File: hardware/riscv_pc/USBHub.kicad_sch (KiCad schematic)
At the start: 8 parts, among them U4 SL2.1A, X1 X49SD12MSD2SC

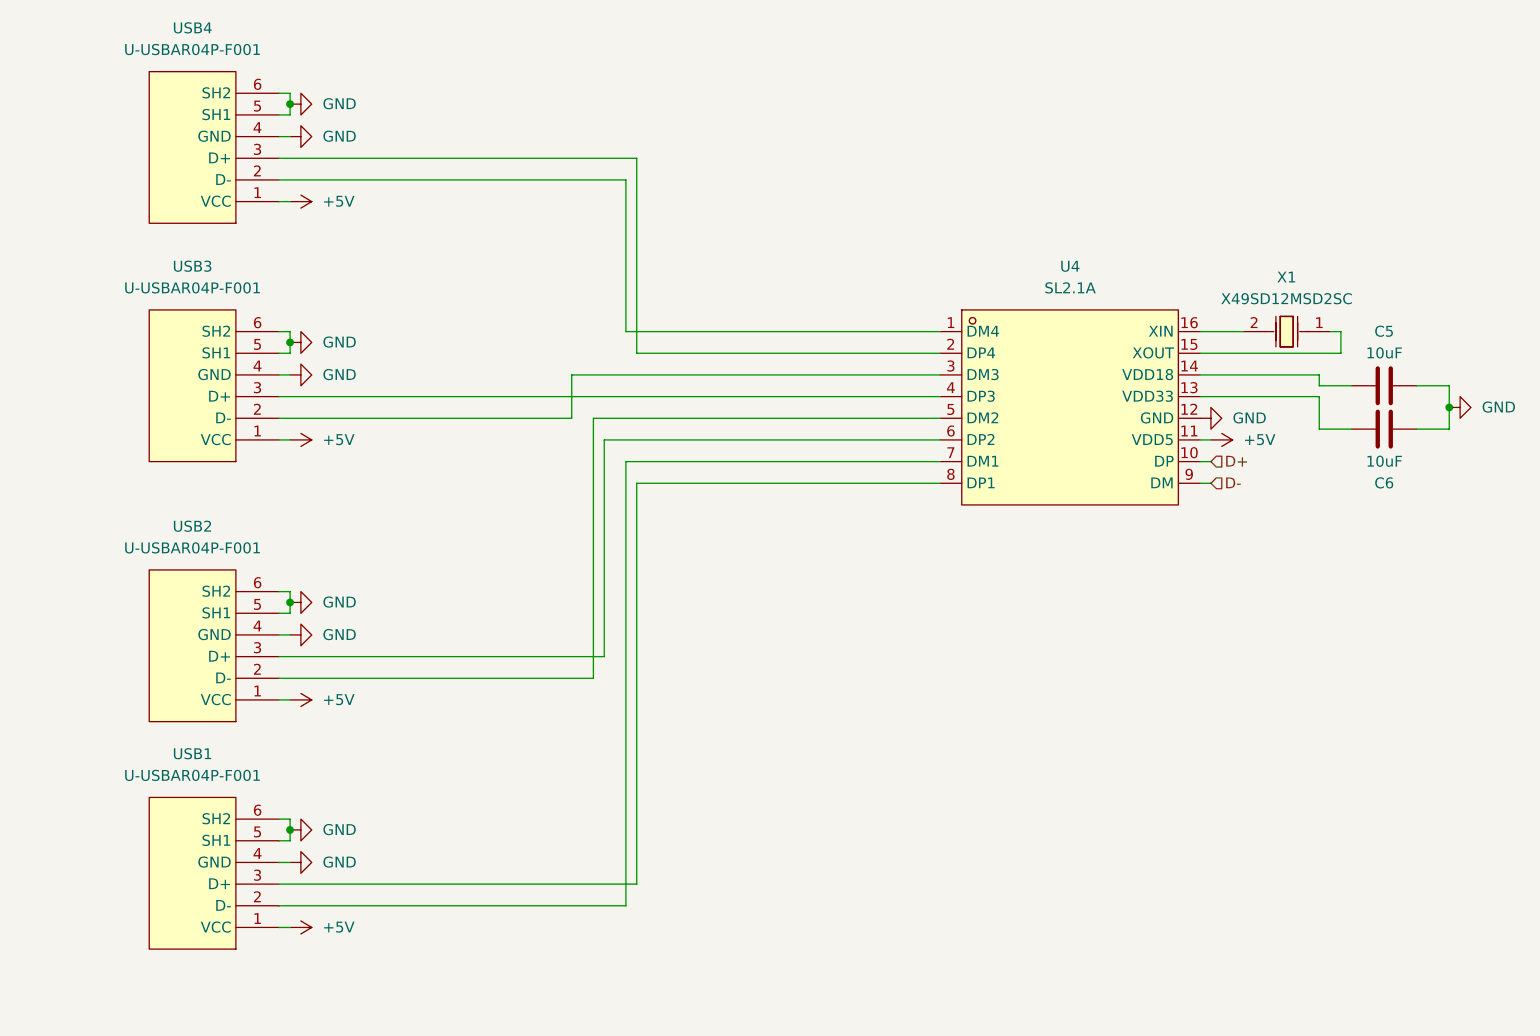
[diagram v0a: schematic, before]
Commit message: Add ESD protection to USB Lines
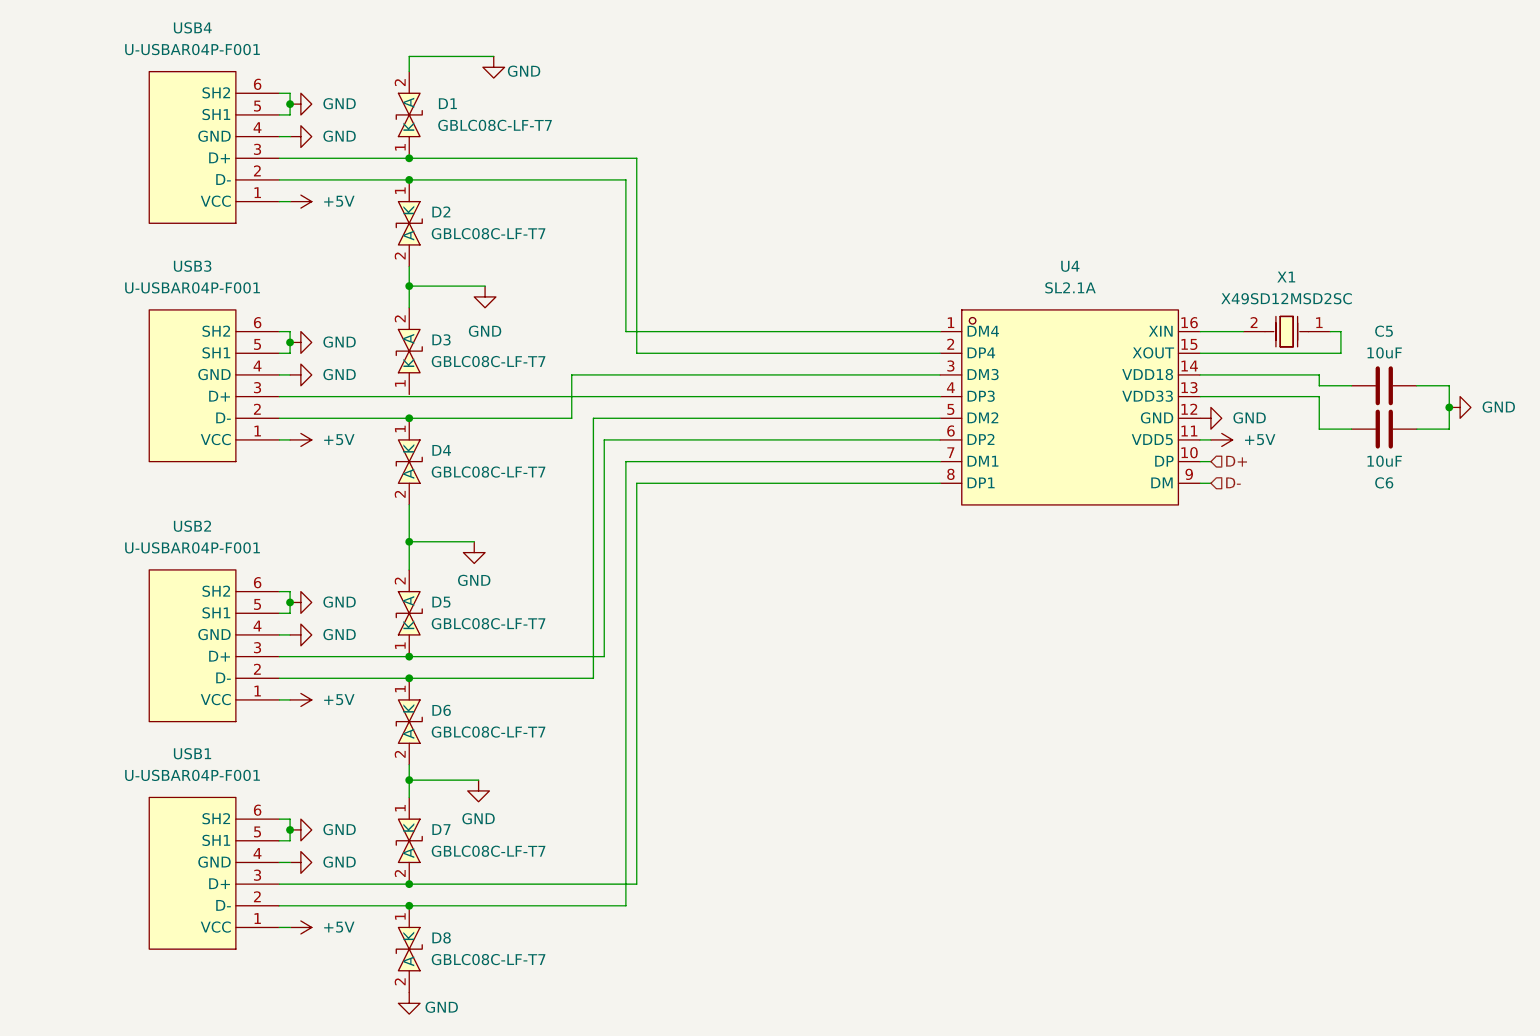
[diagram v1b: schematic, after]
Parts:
- added D1, D2, D3, D4, D5, D6, D7, D8: GBLC08C-LF-T7, easyeda2kicad:SOD-323_L1.8-W1.3-LS2.5-BI, symbol lcsc:GBLC08C-LF-T7
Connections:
- net GND: now also D1.2 (A), D2.2 (A), D3.2 (A), D4.2 (A), D5.2 (A), D6.2 (A), D7.1 (K), D8.2 (A)
- net at U4.7 (DM1), USB1.2 (D-): now also D8.1 (K)
- net at U4.8 (DP1), USB1.3 (D+): now also D7.2 (A)
- net at U4.1 (DM4), USB4.2 (D-): now also D2.1 (K)
- net at U4.2 (DP4), USB4.3 (D+): now also D1.1 (K)
- net at U4.5 (DM2), USB2.2 (D-): now also D6.1 (K)
- net at U4.6 (DP2), USB2.3 (D+): now also D5.1 (K)
- net at U4.3 (DM3), USB3.2 (D-): now also D4.1 (K)

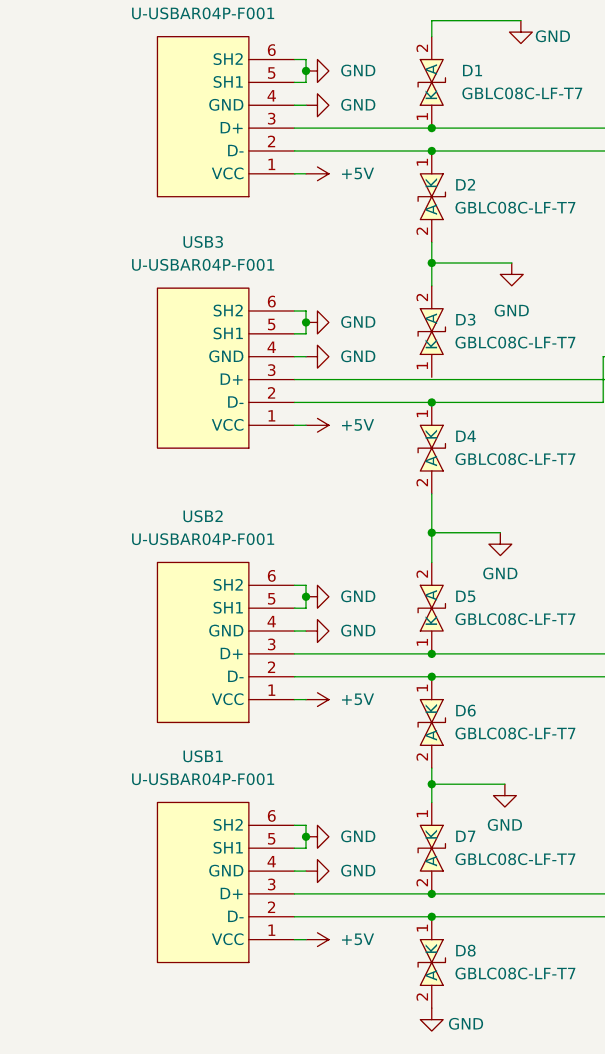
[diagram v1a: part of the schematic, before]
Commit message: Add ESD protection to AUX port
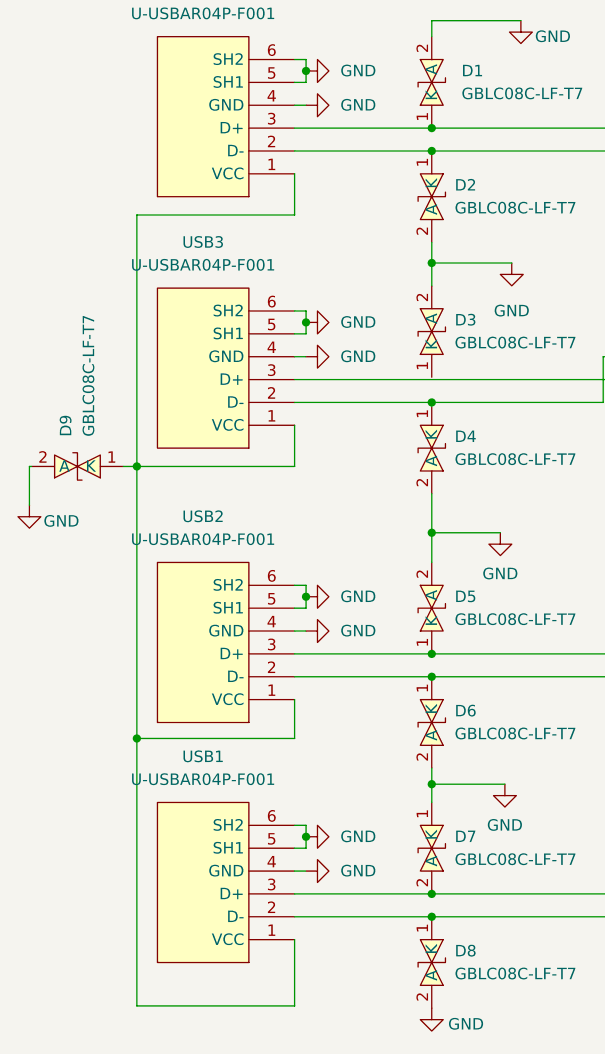
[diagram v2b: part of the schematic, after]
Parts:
- added D9: GBLC08C-LF-T7, easyeda2kicad:SOD-323_L1.8-W1.3-LS2.5-BI, symbol lcsc:GBLC08C-LF-T7
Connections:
- net +5V: no longer USB1.1 (VCC), USB2.1 (VCC), USB3.1 (VCC), USB4.1 (VCC)
- net GND: now also D9.2 (A)
- new net: D9.1 (K), USB1.1 (VCC), USB2.1 (VCC), USB3.1 (VCC), USB4.1 (VCC)
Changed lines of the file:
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@@
   (junction (at 46.99 54.61) (diameter 0) (color 0 0 0 0)
   )
+  (junction (at 28.194 100.838) (diameter 0) (color 0 0 0 0)
+  )
   (junction (at 60.96 118.11) (diameter 0) (color 0 0 0 0)
   )
@@
   (junction (at 60.96 33.02) (diameter 0) (color 0 0 0 0)
   )
+  (junction (at 28.194 70.612) (diameter 0) (color 0 0 0 0)
+  )
+  (wire (pts (xy 28.194 70.612) (xy 28.194 42.672))
+    (stroke (width 0) (type default) (color 0 0 0 0))
+  )
   (wire (pts (xy 46.99 115.57) (xy 45.72 115.57))
     (stroke (width 0) (type default) (color 0 0 0 0))
@@
     (stroke (width 0) (type default) (color 0 0 0 0))
   )
+  (wire (pts (xy 45.72 70.612) (xy 28.194 70.612))
+    (stroke (width 0) (type default) (color 0 0 0 0))
+  )
   (wire (pts (xy 87.63 71.12) (xy 87.63 118.11))
     (stroke (width 0) (type default) (color 0 0 0 0))
   )
+  (wire (pts (xy 45.72 66.04) (xy 45.72 70.612))
+    (stroke (width 0) (type default) (color 0 0 0 0))
+  )
   (wire (pts (xy 60.96 77.978) (xy 68.58 77.978))
     (stroke (width 0) (type default) (color 0 0 0 0))
@@
     (stroke (width 0) (type default) (color 0 0 0 0))
   )
+  (wire (pts (xy 45.72 42.672) (xy 45.72 38.1))
+    (stroke (width 0) (type default) (color 0 0 0 0))
+  )
   (wire (pts (xy 87.63 33.02) (xy 60.96 33.02))
     (stroke (width 0) (type default) (color 0 0 0 0))
@@
     (stroke (width 0) (type default) (color 0 0 0 0))
   )
-  (wire (pts (xy 46.99 123.19) (xy 45.72 123.19))
-    (stroke (width 0) (type default) (color 0 0 0 0))
-  )
   (wire (pts (xy 46.99 54.61) (xy 46.99 55.88))
     (stroke (width 0) (type default) (color 0 0 0 0))
   )
+  (wire (pts (xy 16.256 70.612) (xy 16.51 70.612))
+    (stroke (width 0) (type default) (color 0 0 0 0))
+  )
   (wire (pts (xy 82.55 63.5) (xy 82.55 93.98))
     (stroke (width 0) (type default) (color 0 0 0 0))
@@
     (stroke (width 0) (type default) (color 0 0 0 0))
   )
+  (wire (pts (xy 45.72 96.52) (xy 45.72 100.838))
+    (stroke (width 0) (type default) (color 0 0 0 0))
+  )
   (wire (pts (xy 167.64 58.42) (xy 167.64 59.69))
     (stroke (width 0) (type default) (color 0 0 0 0))
@@
     (stroke (width 0) (type default) (color 0 0 0 0))
   )
+  (wire (pts (xy 45.72 123.19) (xy 45.72 130.556))
+    (stroke (width 0) (type default) (color 0 0 0 0))
+  )
   (wire (pts (xy 46.99 111.76) (xy 46.99 113.03))
     (stroke (width 0) (type default) (color 0 0 0 0))
   )
-  (wire (pts (xy 46.99 38.1) (xy 45.72 38.1))
-    (stroke (width 0) (type default) (color 0 0 0 0))
-  )
   (wire (pts (xy 123.19 66.04) (xy 83.82 66.04))
     (stroke (width 0) (type default) (color 0 0 0 0))
@@
     (stroke (width 0) (type default) (color 0 0 0 0))
   )
+  (wire (pts (xy 28.194 70.612) (xy 28.194 100.838))
+    (stroke (width 0) (type default) (color 0 0 0 0))
+  )
   (wire (pts (xy 167.64 64.77) (xy 171.45 64.77))
     (stroke (width 0) (type default) (color 0 0 0 0))
@@
     (stroke (width 0) (type default) (color 0 0 0 0))
   )
+  (wire (pts (xy 16.256 74.93) (xy 16.256 70.612))
+    (stroke (width 0) (type default) (color 0 0 0 0))
+  )
   (wire (pts (xy 158.75 53.34) (xy 153.67 53.34))
     (stroke (width 0) (type default) (color 0 0 0 0))
   )
+  (wire (pts (xy 26.67 70.612) (xy 28.194 70.612))
+    (stroke (width 0) (type default) (color 0 0 0 0))
+  )
   (wire (pts (xy 123.19 68.58) (xy 86.36 68.58))
     (stroke (width 0) (type default) (color 0 0 0 0))
   )
+  (wire (pts (xy 45.72 100.838) (xy 28.194 100.838))
+    (stroke (width 0) (type default) (color 0 0 0 0))
+  )
   (wire (pts (xy 60.96 104.14) (xy 60.96 105.918))
     (stroke (width 0) (type default) (color 0 0 0 0))
@@
     (stroke (width 0) (type default) (color 0 0 0 0))
   )
+  (wire (pts (xy 45.72 130.556) (xy 28.194 130.556))
+    (stroke (width 0) (type default) (color 0 0 0 0))
+  )
   (wire (pts (xy 45.72 83.82) (xy 46.99 83.82))
     (stroke (width 0) (type default) (color 0 0 0 0))
   )
+  (wire (pts (xy 28.194 42.672) (xy 45.72 42.672))
+    (stroke (width 0) (type default) (color 0 0 0 0))
+  )
   (wire (pts (xy 46.99 30.48) (xy 45.72 30.48))
     (stroke (width 0) (type default) (color 0 0 0 0))
@@
     (stroke (width 0) (type default) (color 0 0 0 0))
   )
-  (wire (pts (xy 46.99 96.52) (xy 45.72 96.52))
-    (stroke (width 0) (type default) (color 0 0 0 0))
-  )
   (wire (pts (xy 60.96 48.006) (xy 69.85 48.006))
     (stroke (width 0) (type default) (color 0 0 0 0))
@@
     (stroke (width 0) (type default) (color 0 0 0 0))
   )
-  (wire (pts (xy 46.99 66.04) (xy 45.72 66.04))
+  (wire (pts (xy 28.194 100.838) (xy 28.194 130.556))
     (stroke (width 0) (type default) (color 0 0 0 0))
   )
@@
     )
     (property "Datasheet" "" (id 3) (at 70.866 21.082 0)
-      (effects (font (size 1.27 1.27)) hide)
-    )
-    (pin "1")
-  )
-  (symbol (lib_id "power:+5V") (at 46.99 123.19 270) (unit 1)
-    (in_bom yes) (on_board yes) (fields_autoplaced)
-    (property "Reference" "#PWR0123" (id 0) (at 43.18 123.19 0)
-      (effects (font (size 1.27 1.27)) hide)
-    )
-    (property "Value" "+5V" (id 1) (at 50.8 123.1899 90)
-      (effects (font (size 1.27 1.27)) (justify left))
-    )
-    (property "Footprint" "" (id 2) (at 46.99 123.19 0)
-      (effects (font (size 1.27 1.27)) hide)
-    )
-    (property "Datasheet" "" (id 3) (at 46.99 123.19 0)
       (effects (font (size 1.27 1.27)) hide)
     )
@@
     (pin "2")
   )
-  (symbol (lib_id "power:+5V") (at 46.99 38.1 270) (unit 1)
-    (in_bom yes) (on_board yes) (fields_autoplaced)
-    (property "Reference" "#PWR0128" (id 0) (at 43.18 38.1 0)
-      (effects (font (size 1.27 1.27)) hide)
-    )
-    (property "Value" "+5V" (id 1) (at 50.8 38.0999 90)
-      (effects (font (size 1.27 1.27)) (justify left))
-    )
-    (property "Footprint" "" (id 2) (at 46.99 38.1 0)
-      (effects (font (size 1.27 1.27)) hide)
-    )
-    (property "Datasheet" "" (id 3) (at 46.99 38.1 0)
+  (symbol (lib_id "power:GND") (at 16.256 74.93 0) (unit 1)
+    (in_bom yes) (on_board yes)
+    (property "Reference" "#PWR012" (id 0) (at 16.256 81.28 0)
+      (effects (font (size 1.27 1.27)) hide)
+    )
+    (property "Value" "GND" (id 1) (at 19.812 76.708 0))
+    (property "Footprint" "" (id 2) (at 16.256 74.93 0)
+      (effects (font (size 1.27 1.27)) hide)
+    )
+    (property "Datasheet" "" (id 3) (at 16.256 74.93 0)
       (effects (font (size 1.27 1.27)) hide)
     )
@@
     (pin "2")
   )
+  (symbol (lib_id "lcsc:GBLC08C-LF-T7") (at 21.59 70.612 180) (unit 1)
+    (in_bom yes) (on_board yes) (fields_autoplaced)
+    (property "Reference" "D9" (id 0) (at 20.3199 67.31 90)
+      (effects (font (size 1.27 1.27)) (justify right))
+    )
+    (property "Value" "GBLC08C-LF-T7" (id 1) (at 22.8599 67.31 90)
+      (effects (font (size 1.27 1.27)) (justify right))
+    )
+    (property "Footprint" "easyeda2kicad:SOD-323_L1.8-W1.3-LS2.5-BI" (id 2) (at 21.59 62.992 0)
+      (effects (font (size 1.27 1.27)) hide)
+    )
+    (property "Datasheet" "https://lcsc.com/product-detail/Others_ProTek-Devices-GBLC08C-LF-T7_C282422.html" (id 3) (at 21.59 60.452 0)
+      (effects (font (size 1.27 1.27)) hide)
+    )
+    (property "Manufacturer" "PROTEK" (id 4) (at 21.59 57.912 0)
+      (effects (font (size 1.27 1.27)) hide)
+    )
+    (property "LCSC Part" "C282422" (id 5) (at 21.59 55.372 0)
+      (effects (font (size 1.27 1.27)) hide)
+    )
+    (property "JLC Part" "Extended Part" (id 6) (at 21.59 52.832 0)
+      (effects (font (size 1.27 1.27)) hide)
+    )
+    (pin "1")
+    (pin "2")
+  )
   (symbol (lib_id "power:+5V") (at 154.94 66.04 270) (unit 1)
     (in_bom yes) (on_board yes) (fields_autoplaced)
@@
     (pin "1")
     (pin "2")
-  )
-  (symbol (lib_id "power:+5V") (at 46.99 96.52 270) (unit 1)
-    (in_bom yes) (on_board yes) (fields_autoplaced)
-    (property "Reference" "#PWR0122" (id 0) (at 43.18 96.52 0)
-      (effects (font (size 1.27 1.27)) hide)
-    )
-    (property "Value" "+5V" (id 1) (at 50.8 96.5199 90)
-      (effects (font (size 1.27 1.27)) (justify left))
-    )
-    (property "Footprint" "" (id 2) (at 46.99 96.52 0)
-      (effects (font (size 1.27 1.27)) hide)
-    )
-    (property "Datasheet" "" (id 3) (at 46.99 96.52 0)
-      (effects (font (size 1.27 1.27)) hide)
-    )
-    (pin "1")
   )
   (symbol (lib_id "power:GND") (at 68.58 77.978 0) (unit 1)
@@
       (effects (font (size 1.27 1.27)) hide)
     )
-    (pin "1")
-  )
-  (symbol (lib_id "power:+5V") (at 46.99 66.04 270) (unit 1)
-    (in_bom yes) (on_board yes) (fields_autoplaced)
-    (property "Reference" "#PWR0127" (id 0) (at 43.18 66.04 0)
-      (effects (font (size 1.27 1.27)) hide)
-    )
-    (property "Value" "+5V" (id 1) (at 50.8 66.0399 90)
-      (effects (font (size 1.27 1.27)) (justify left))
-    )
-    (property "Footprint" "" (id 2) (at 46.99 66.04 0)
-      (effects (font (size 1.27 1.27)) hide)
-    )
-    (property "Datasheet" "" (id 3) (at 46.99 66.04 0)
-      (effects (font (size 1.27 1.27)) hide)
-    )

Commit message: Create PCB
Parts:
- removed C5, C6: 10uF, symbol Device:C
- added C? (x2): CL31A106KBHNNNE, easyeda2kicad:C1206, symbol lcsc:CL31A106KBHNNNE
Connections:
- net GND: now also C?.2, C?.2
- net at U4.14 (VDD18): now also C?.1
- net at U4.13 (VDD33): now also C?.1
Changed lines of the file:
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@@
     (pin "1")
-  )
-  (symbol (lib_id "Device:C") (at 175.26 59.69 90) (unit 1)
-    (in_bom yes) (on_board yes)
-    (property "Reference" "C5" (id 0) (at 175.26 53.34 90))
-    (property "Value" "10uF" (id 1) (at 175.26 55.88 90))
-    (property "Footprint" "" (id 2) (at 179.07 58.7248 0)
-      (effects (font (size 1.27 1.27)) hide)
-    )
-    (property "Datasheet" "~" (id 3) (at 175.26 59.69 0)
-      (effects (font (size 1.27 1.27)) hide)
-    )
-    (pin "1")
-    (pin "2")
   )
   (symbol (lib_id "lcsc:GBLC08C-LF-T7") (at 21.59 70.612 180) (unit 1)
@@
     (pin "5")
     (pin "6")
-  )
-  (symbol (lib_id "Device:C") (at 175.26 64.77 90) (unit 1)
-    (in_bom yes) (on_board yes)
-    (property "Reference" "C6" (id 0) (at 175.26 71.12 90))
-    (property "Value" "10uF" (id 1) (at 175.26 68.58 90))
-    (property "Footprint" "" (id 2) (at 179.07 63.8048 0)
-      (effects (font (size 1.27 1.27)) hide)
-    )
-    (property "Datasheet" "~" (id 3) (at 175.26 64.77 0)
-      (effects (font (size 1.27 1.27)) hide)
-    )
-    (pin "1")
-    (pin "2")
   )
   (symbol (lib_id "power:GND") (at 68.58 77.978 0) (unit 1)
@@
     (pin "1")
   )
+  (symbol (lib_id "lcsc:CL31A106KBHNNNE") (at 175.26 64.77 0) (unit 1)
+    (in_bom yes) (on_board yes)
+    (property "Reference" "C?" (id 0) (at 175.26 67.818 0))
+    (property "Value" "CL31A106KBHNNNE" (id 1) (at 175.26 59.69 0)
+      (effects (font (size 1.27 1.27)) hide)
+    )
+    (property "Footprint" "easyeda2kicad:C1206" (id 2) (at 175.26 72.39 0)
+      (effects (font (size 1.27 1.27)) hide)
+    )
+    (property "Datasheet" "https://lcsc.com/product-detail/Multilayer-Ceramic-Capacitors-MLCC-SMD-SMT_SAMSUNG_CL31A106KBHNNNE_10uF-106-10-50V_C13585.html" (id 3) (at 175.26 74.93 0)
+      (effects (font (size 1.27 1.27)) hide)
+    )
+    (property "Manufacturer" "SAMSUNG(三星)" (id 4) (at 175.26 77.47 0)
+      (effects (font (size 1.27 1.27)) hide)
+    )
+    (property "LCSC Part" "C13585" (id 5) (at 175.26 80.01 0)
+      (effects (font (size 1.27 1.27)) hide)
+    )
+    (property "JLC Part" "Basic Part" (id 6) (at 175.26 82.55 0)
+      (effects (font (size 1.27 1.27)) hide)
+    )
+    (pin "1")
+    (pin "2")
+  )
   (symbol (lib_id "power:GND") (at 46.99 26.67 90) (unit 1)
     (in_bom yes) (on_board yes) (fields_autoplaced)
@@
     (pin "1")
   )
+  (symbol (lib_id "lcsc:CL31A106KBHNNNE") (at 175.26 59.69 0) (unit 1)
+    (in_bom yes) (on_board yes)
+    (property "Reference" "C?" (id 0) (at 175.26 56.642 0))
+    (property "Value" "CL31A106KBHNNNE" (id 1) (at 175.26 54.61 0)
+      (effects (font (size 1.27 1.27)) hide)
+    )
+    (property "Footprint" "easyeda2kicad:C1206" (id 2) (at 175.26 67.31 0)
+      (effects (font (size 1.27 1.27)) hide)
+    )
+    (property "Datasheet" "https://lcsc.com/product-detail/Multilayer-Ceramic-Capacitors-MLCC-SMD-SMT_SAMSUNG_CL31A106KBHNNNE_10uF-106-10-50V_C13585.html" (id 3) (at 175.26 69.85 0)
+      (effects (font (size 1.27 1.27)) hide)
+    )
+    (property "Manufacturer" "SAMSUNG(三星)" (id 4) (at 175.26 72.39 0)
+      (effects (font (size 1.27 1.27)) hide)
+    )
+    (property "LCSC Part" "C13585" (id 5) (at 175.26 74.93 0)
+      (effects (font (size 1.27 1.27)) hide)
+    )
+    (property "JLC Part" "Basic Part" (id 6) (at 175.26 77.47 0)
+      (effects (font (size 1.27 1.27)) hide)
+    )
+    (pin "1")
+    (pin "2")
+  )
 )
